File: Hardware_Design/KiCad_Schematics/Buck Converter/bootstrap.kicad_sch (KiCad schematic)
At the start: 6 parts, among them Q1 2N7002

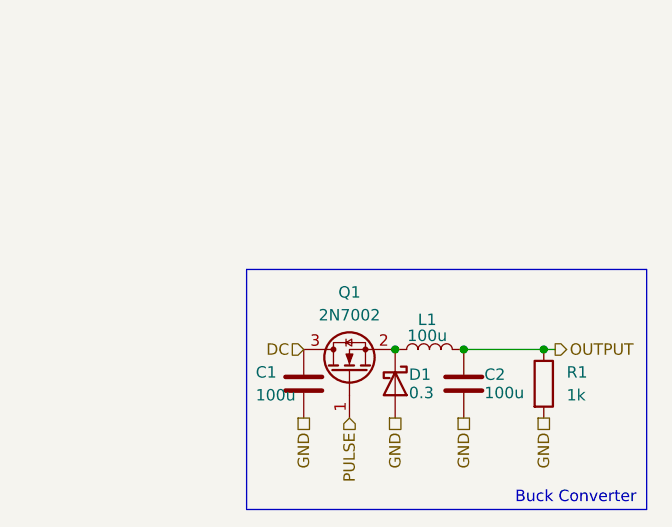
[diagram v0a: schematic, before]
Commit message: init: initialize new circuit for the previous problem
Started the Bootstrap Driver circuit to solve the previous problem. This way, the NMOSFET will be able to operate in full saturation.
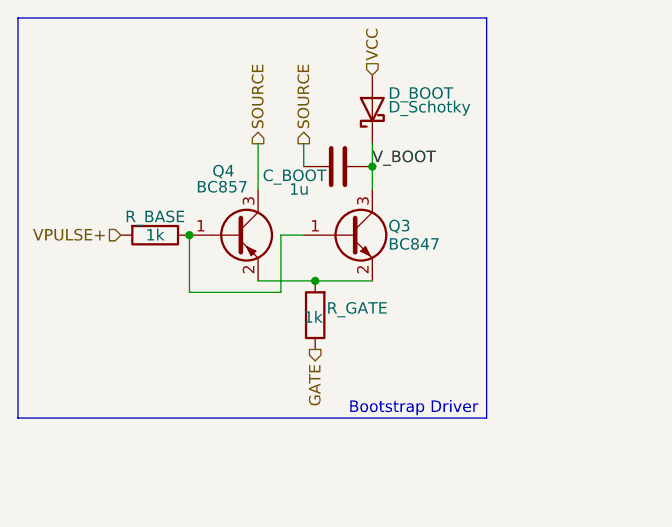
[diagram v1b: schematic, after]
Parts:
- removed C1, C2: 100u, Capacitor_THT:CP_Radial_D4.0mm_P1.50mm, symbol Device:C
- removed D1: 0.3, Diode_THT:D_A-405_P7.62mm_Horizontal, symbol Device:D_Schottky
- removed L1: 100u, Inductor_THT:L_Radial_D6.0mm_P4.00mm, symbol Device:L
- removed Q1: 2N7002, Package_TO_SOT_THT:TO-220-3_Vertical, symbol Transistor_FET:2N7002
- removed R1: 1k, Resistor_THT:R_Axial_DIN0204_L3.6mm_D1.6mm_P5.08mm_Horizontal, symbol Device:R
- added C_BOOT: 1u, symbol Device:C
- added D_BOOT: D_Schotky, symbol Device:D_Schottky
- added Q3: BC847, Package_TO_SOT_SMD:SOT-23, symbol Transistor_BJT:BC847
- added Q4: BC857, Package_TO_SOT_SMD:SOT-23, symbol Transistor_BJT:BC857
- added R_BASE, R_GATE: 1k, symbol Device:R
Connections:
- new net: Q3.1 (B), Q4.1 (B), R_BASE.1
- new net: Q3.2 (E), Q4.2 (E), R_GATE.2
- new net GATE: R_GATE.1
- new net SOURCE: C_BOOT.1, Q4.3 (C)
- new net VCC: D_BOOT.2 (A)
- new net VPULSE+: R_BASE.2
- new net V_BOOT: C_BOOT.2, D_BOOT.1 (K), Q3.3 (C)
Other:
- note added: "Bootstrap Driver"
- note removed: "Buck Converter"

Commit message: Update designs but continue problems...
Added a Bootstrap circuit to bring the MOSFET from a Linear Regulator state to a Buck Converter state, but the problem is still not resolved. While it should yield a value close to 6V when the Duty Cycle is at 50% and a 12V input is applied, it yields 4V, and the graph is not correct. Work on the problem will continue.
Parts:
- R_GATE2: renamed from R_GATE; value 1k -> 10
- renumbered C_BOOT to C_BOOT2, D_BOOT to D_BOOT2, Q4 to Q5, Q3 to Q6, R_BASE to R_BASE2
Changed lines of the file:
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@@
 		(in_pos_files yes)
 		(dnp no)
-		(property "Reference" "D_BOOT"
+		(property "Reference" "D_BOOT2"
 			(at 128.778 57.912 90)
 			(show_name no)
@@
 			(project "buck_converter"
 				(path "/e6ad1407-9765-4ff4-965d-dd4ca2472230/99839e64-c2cf-4e0f-8bc6-cadc19dd91e8"
-					(reference "D_BOOT")
+					(reference "D_BOOT2")
 					(unit 1)
 				)
@@
 		(in_pos_files yes)
 		(dnp no)
-		(property "Reference" "Q4"
+		(property "Reference" "Q5"
 			(at 109.22 66.548 0)
 			(show_name no)
@@
 			(project "buck_converter"
 				(path "/e6ad1407-9765-4ff4-965d-dd4ca2472230/99839e64-c2cf-4e0f-8bc6-cadc19dd91e8"
-					(reference "Q4")
+					(reference "Q5")
 					(unit 1)
 				)
@@
 		(in_pos_files yes)
 		(dnp no)
-		(property "Reference" "R_BASE"
+		(property "Reference" "R_BASE2"
 			(at 102.87 71.628 90)
 			(show_name no)
@@
 			(project "buck_converter"
 				(path "/e6ad1407-9765-4ff4-965d-dd4ca2472230/99839e64-c2cf-4e0f-8bc6-cadc19dd91e8"
-					(reference "R_BASE")
+					(reference "R_BASE2")
 					(unit 1)
 				)
@@
 		(in_pos_files yes)
 		(dnp no)
-		(property "Reference" "R_GATE"
+		(property "Reference" "R_GATE2"
 			(at 121.92 81.788 0)
 			(show_name no)
@@
 			)
 		)
-		(property "Value" "1k"
-			(at 119.38 82.804 0)
+		(property "Value" "10"
+			(at 124.46 83.566 0)
 			(show_name no)
 			(do_not_autoplace no)
@@
 			(project "buck_converter"
 				(path "/e6ad1407-9765-4ff4-965d-dd4ca2472230/99839e64-c2cf-4e0f-8bc6-cadc19dd91e8"
-					(reference "R_GATE")
+					(reference "R_GATE2")
 					(unit 1)
 				)
@@
 		(in_pos_files yes)
 		(dnp no)
-		(property "Reference" "C_BOOT"
+		(property "Reference" "C_BOOT2"
 			(at 118.364 67.056 90)
 			(show_name no)
@@
 			(project "buck_converter"
 				(path "/e6ad1407-9765-4ff4-965d-dd4ca2472230/99839e64-c2cf-4e0f-8bc6-cadc19dd91e8"
-					(reference "C_BOOT")
+					(reference "C_BOOT2")
 					(unit 1)
 				)
@@
 		(in_pos_files yes)
 		(dnp no)
-		(property "Reference" "Q3"
+		(property "Reference" "Q6"
 			(at 128.778 72.644 0)
 			(show_name no)
@@
 			(project "buck_converter"
 				(path "/e6ad1407-9765-4ff4-965d-dd4ca2472230/99839e64-c2cf-4e0f-8bc6-cadc19dd91e8"
-					(reference "Q3")
+					(reference "Q6")
 					(unit 1)
 				)
